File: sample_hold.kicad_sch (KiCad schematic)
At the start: 46 parts, among them K21 G6K-2FY, 5V, Q21 AO3400A, Q22 AO3401A, Q23 AO3400A, Q24 AO3400A, Q25 AO3400A, Q26 AO3400A, Q27 AO3400A, Q28 BSS139, Q29 BSS139, U21 OPA828DGN, U22 OPA2197D, U23 TLV9352D

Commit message: More component metadata.
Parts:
- C202, C211: LCSC (none) -> C14858; Stock (none) -> JLC
- C203, C204, C205, C206, C207, C208, C209, C210, C212, D21, D22, D23, L21, Q21, Q22, Q23, Q24, Q25, Q26, Q27, R201, R203, R204, R205, R206, R208, R209, R210, R211, R215, R216, U21: Stock (none) -> JLC
- JP1: Stock (none) -> Board
- K21: Stock (none) -> LCSC?
- Q28, Q29: Stock (none) -> ?; now left out of the parts list
- R202, R266: footprint Resistor_SMD:R_0402_1005Metric -> Resistor_SMD:R_0603_1608Metric; LCSC (none) -> C25811; Stock (none) -> JLC
- R212: LCSC (none) -> C4190; Stock (none) -> JLC
- R213: LCSC (none) -> C25819; Stock (none) -> JLC
- R214: LCSC (none) -> C4211; Stock (none) -> JLC
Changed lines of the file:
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@@
 			)
 		)
-		(property "Stock" ""
+		(property "Stock" "JLC"
 			(at 177.8 36.83 0)
 			(effects
@@
 			)
 		)
-		(property "Stock" ""
+		(property "Stock" "JLC"
 			(at 106.68 39.37 0)
 			(effects
@@
 			)
 		)
-		(property "Stock" ""
+		(property "Stock" "JLC"
 			(at 161.29 83.82 0)
 			(effects
@@
 			)
 		)
-		(property "Stock" ""
+		(property "Stock" "JLC"
 			(at 85.09 77.47 90)
 			(effects
@@
 			)
 		)
-		(property "Stock" ""
+		(property "Stock" "JLC"
 			(at 78.74 31.75 0)
 			(effects
@@
 			)
 		)
-		(property "Footprint" "Resistor_SMD:R_0402_1005Metric"
+		(property "Footprint" "Resistor_SMD:R_0603_1608Metric"
 			(at 113.03 75.692 90)
 			(effects
@@
 			)
 		)
-		(property "LCSC" ""
+		(property "LCSC" "C25811"
 			(at 113.03 77.47 90)
 			(effects
@@
 			)
 		)
-		(property "Stock" ""
+		(property "Stock" "JLC"
 			(at 113.03 77.47 90)
 			(effects
@@
 			)
 		)
-		(property "Stock" ""
+		(property "Stock" "JLC"
 			(at 78.74 39.37 0)
 			(effects
@@
 			)
 		)
-		(property "Stock" ""
+		(property "Stock" "JLC"
 			(at 156.21 31.75 0)
 			(effects
@@
 		(unit 1)
 		(exclude_from_sim no)
-		(in_bom yes)
+		(in_bom no)
 		(on_board yes)
 		(dnp no)
@@
 			)
 		)
+		(property "Stock" "?"
+			(at 173.99 68.58 90)
+			(effects
+				(font
+					(size 1.27 1.27)
+				)
+				(hide yes)
+			)
+		)
 		(pin "2"
 		)
@@
 			)
 		)
-		(property "LCSC" ""
+		(property "LCSC" "C4211"
 			(at 127 90.17 90)
 			(effects
@@
 			)
 		)
-		(property "Stock" ""
+		(property "Stock" "JLC"
 			(at 127 90.17 90)
 			(effects
@@
 			)
 		)
-		(property "Stock" ""
+		(property "Stock" "JLC"
 			(at 74.93 105.41 0)
 			(effects
@@
 			)
 		)
-		(property "Stock" ""
+		(property "Stock" "JLC"
 			(at 96.52 97.79 90)
 			(effects
@@
 			)
 		)
-		(property "Stock" ""
+		(property "Stock" "JLC"
 			(at 170.18 41.91 0)
 			(effects
@@
 			)
 		)
-		(property "Stock" ""
+		(property "Stock" "Board"
 			(at 92.71 92.71 0)
 			(effects
@@
 			)
 		)
-		(property "Stock" ""
+		(property "Stock" "JLC"
 			(at 138.43 63.5 90)
 			(effects
@@
 			)
 		)
-		(property "Footprint" "Resistor_SMD:R_0402_1005Metric"
+		(property "Footprint" "Resistor_SMD:R_0603_1608Metric"
 			(at 113.03 54.102 90)
 			(effects
@@
 			)
 		)
-		(property "LCSC" ""
+		(property "LCSC" "C25811"
 			(at 113.03 55.88 90)
 			(effects
@@
 			)
 		)
-		(property "Stock" ""
+		(property "Stock" "JLC"
 			(at 113.03 55.88 90)
 			(effects
@@
 			)
 		)
-		(property "LCSC" ""
+		(property "LCSC" "C14858"
 			(at 105.41 73.66 0)
 			(effects
@@
 			)
 		)
-		(property "Stock" ""
+		(property "Stock" "JLC"
 			(at 105.41 73.66 0)
 			(effects
@@
 			)
 		)
-		(property "Stock" ""
+		(property "Stock" "LCSC?"
 			(at 151.13 74.93 90)
 			(effects
@@
 			)
 		)
-		(property "Stock" ""
+		(property "Stock" "JLC"
 			(at 215.9 78.74 90)
 			(effects
@@
 			)
 		)
-		(property "Stock" ""
+		(property "Stock" "JLC"
 			(at 181.61 66.04 90)
 			(effects
@@
 			)
 		)
-		(property "Stock" ""
+		(property "Stock" "LCSC?"
 			(at 156.21 63.5 90)
 			(effects
@@
 			)
 		)
-		(property "Stock" ""
+		(property "Stock" "JLC"
 			(at 184.15 41.91 0)
 			(effects
@@
 			)
 		)
-		(property "Stock" ""
+		(property "Stock" "JLC"
 			(at 100.33 31.75 0)
 			(effects
@@
 			)
 		)
-		(property "Stock" ""
+		(property "Stock" "JLC"
 			(at 138.43 69.85 90)
 			(effects
@@
 			)
 		)
-		(property "Stock" ""
+		(property "Stock" "JLC"
 			(at 181.61 31.75 90)
 			(effects
@@
 			)
 		)
-		(property "LCSC" ""
+		(property "LCSC" "C25819"
 			(at 114.3 97.79 90)
 			(effects
@@
 			)
 		)
-		(property "Stock" ""
+		(property "Stock" "JLC"
 			(at 114.3 97.79 90)
 			(effects
@@
 			)
 		)
-		(property "Stock" ""
+		(property "Stock" "JLC"
 			(at 106.68 31.75 0)
 			(effects
@@
 			)
 		)
-		(property "Stock" ""
+		(property "Stock" "JLC"
 			(at 161.29 91.44 0)
 			(effects
@@
 			)
 		)
-		(property "Stock" ""
+		(property "Stock" "JLC"
 			(at 171.45 83.82 0)
 			(effects
@@
 			)
 		)
-		(property "Stock" ""
+		(property "Stock" "LCSC?"
 			(at 156.21 41.91 90)
 			(effects
@@
 			)
 		)
-		(property "Stock" ""
+		(property "Stock" "JLC"
 			(at 215.9 68.58 90)
 			(effects
@@
 			)
 		)
-		(property "Stock" ""
+		(property "Stock" "JLC"
 			(at 189.23 31.75 0)
 			(effects
@@
 			)
 		)
-		(property "LCSC" ""
+		(property "LCSC" "C4190"
 			(at 101.6 92.71 90)
 			(effects
@@
 			)
 		)
-		(property "Stock" ""
+		(property "Stock" "JLC"
 			(at 101.6 92.71 90)
 			(effects
@@
 			)
 		)
-		(property "Stock" ""
+		(property "Stock" "JLC"
 			(at 170.18 27.94 90)
 			(effects
@@
 			)
 		)
-		(property "Stock" ""
+		(property "Stock" "JLC"
 			(at 142.24 41.91 0)
 			(effects
@@
 			)
 		)
-		(property "Stock" ""
+		(property "Stock" "JLC"
 			(at 100.33 39.37 0)
 			(effects
@@
 			)
 		)
-		(property "Stock" ""
+		(property "Stock" "JLC"
 			(at 187.96 45.72 90)
 			(effects
@@
 			)
 		)
-		(property "Stock" ""
+		(property "Stock" "JLC"
 			(at 203.2 68.58 0)
 			(effects
@@
 			)
 		)
-		(property "Stock" ""
+		(property "Stock" "JLC"
 			(at 138.43 58.42 90)
 			(effects
@@
 			)
 		)
-		(property "Stock" ""
+		(property "Stock" "JLC"
 			(at 171.45 91.44 0)
 			(effects
@@
 			)
 		)
-		(property "Stock" ""
+		(property "Stock" "JLC"
 			(at 74.93 97.79 0)
 			(effects
@@
 			)
 		)
-		(property "LCSC" ""
+		(property "LCSC" "C14858"
 			(at 210.82 73.66 0)
 			(effects
@@
 			)
 		)
-		(property "Stock" ""
+		(property "Stock" "JLC"
 			(at 210.82 73.66 0)
 			(effects
@@
 			)
 		)
-		(property "Stock" ""
+		(property "Stock" "JLC"
 			(at 138.43 74.93 90)
 			(effects
@@
 			)
 		)
-		(property "Stock" ""
+		(property "Stock" "JLC"
 			(at 134.62 45.72 0)
 			(effects
@@
 		(unit 1)
 		(exclude_from_sim no)
-		(in_bom yes)
+		(in_bom no)
 		(on_board yes)
 		(dnp no)
@@
 			(effects
 				(font
+					(size 1.27 1.27)
+				)
+				(hide yes)
+			)
+		)
+		(property "Stock" "?"
+			(at 189.23 63.5 90)
+			(effects
+				(font

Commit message: Front panel
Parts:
- C211: value 0n1 -> 10n; LCSC C14858 -> C307500
- R201: value 16k -> 15k; footprint Resistor_SMD:R_0603_1608Metric -> Resistor_SMD:R_0402_1005Metric; LCSC C22818 -> C25756
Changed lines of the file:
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@@
 			)
 		)
-		(property "Value" "16k"
+		(property "Value" "15k"
 			(at 85.09 77.47 90)
 			(effects
@@
 			)
 		)
-		(property "Footprint" "Resistor_SMD:R_0603_1608Metric"
+		(property "Footprint" "Resistor_SMD:R_0402_1005Metric"
 			(at 85.09 75.692 90)
 			(effects
@@
 			)
 		)
-		(property "LCSC" "C22818"
+		(property "LCSC" "C25756"
 			(at 85.09 77.47 90)
 			(effects
@@
 			)
 		)
-		(property "Value" "0n1"
+		(property "Value" "10n"
 			(at 210.82 75.692 0)
 			(effects
@@
 			)
 		)
-		(property "LCSC" "C14858"
+		(property "LCSC" "C307500"
 			(at 210.82 73.66 0)
 			(effects

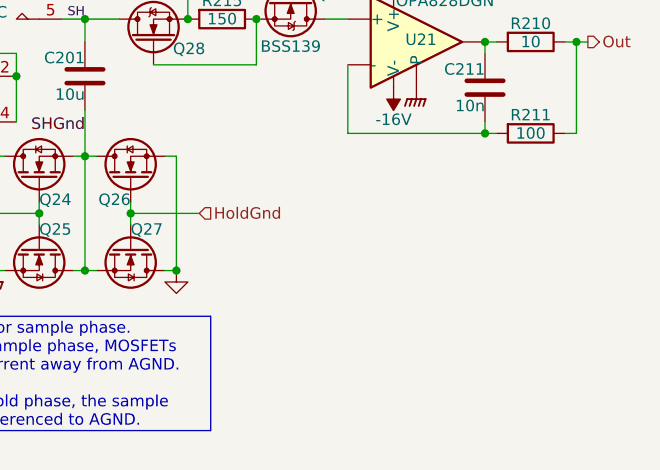
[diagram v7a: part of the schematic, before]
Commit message: Change some footprints.
Mounting holes for covers.
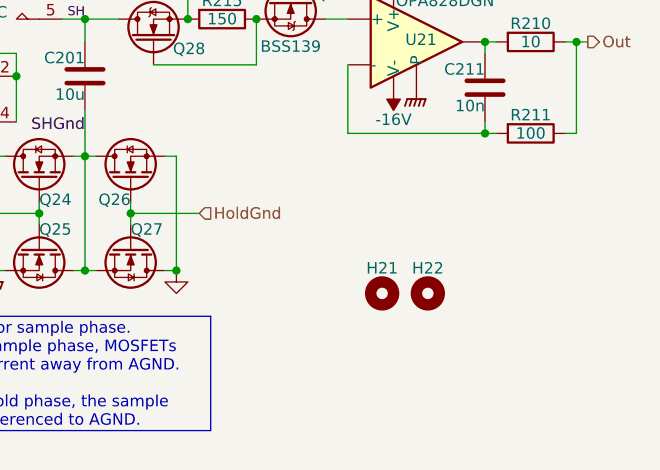
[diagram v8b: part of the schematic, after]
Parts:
- added H21, H22: MountingHole, Parts:Hole_1.5mm_Unplated, symbol Mechanical:MountingHole
- U21: footprint Parts:OPA828DGN -> Parts:SOIC-8_3.9x4.9mm_EP; Stock JLC -> (none); now left out of the parts list
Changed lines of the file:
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@@
+	)
+	(symbol
+		(lib_id "Mechanical:MountingHole")
+		(at 204.47 96.52 0)
+		(unit 1)
+		(exclude_from_sim no)
+		(in_bom no)
+		(on_board yes)
+		(dnp no)
+		(property "Reference" "H22"
+			(at 204.47 93.726 0)
+			(effects
+				(font
+					(size 1.27 1.27)
+				)
+			)
+		)
+		(property "Value" "MountingHole"
+			(at 204.47 93.345 0)
+			(effects
+				(font
+					(size 1.27 1.27)
+				)
+				(hide yes)
+			)
+		)
+		(property "Footprint" "Parts:Hole_1.5mm_Unplated"
+			(at 204.47 96.52 0)
+			(effects
+				(font
+					(size 1.27 1.27)
+				)
+				(hide yes)
+			)
+		)
+		(property "Datasheet" "~"
+			(at 204.47 96.52 0)
+			(effects
+				(font
+					(size 1.27 1.27)
+				)
+				(hide yes)
+			)
+		)
+		(property "Description" "Mounting Hole without connection"
+			(at 204.47 96.52 0)
+			(effects
+				(font
+					(size 1.27 1.27)
+				)
+				(hide yes)
+			)
+		)
+		(instances
+			(project "lincal"
+				(path "/b054cef4-39e3-49d8-aff0-7ba5a206c187/6f91b1d1-06a0-428d-b546-bc9bd4fa19a0"
+					(reference "H26")
+					(unit 1)
+				)
+				(path "/b054cef4-39e3-49d8-aff0-7ba5a206c187/8eaf15be-2df7-401b-a518-33a048754894"
+					(reference "H22")
+					(unit 1)
+				)
+			)
+		)
 	)
 	(symbol
@@
 		(unit 1)
 		(exclude_from_sim no)
-		(in_bom yes)
+		(in_bom no)
 		(on_board yes)
 		(dnp no)
@@
 			)
 		)
-		(property "Footprint" "Parts:OPA828DGN"
+		(property "Footprint" "Parts:SOIC-8_3.9x4.9mm_EP"
 			(at 200.66 73.66 0)
 			(effects
@@
 			)
 		)
-		(property "Stock" "JLC"
+		(property "Stock" ""
 			(at 203.2 68.58 0)
 			(effects
@@
 					(unit 1)
 				)
+			)
+		)
+	)
+	(symbol
+		(lib_id "Mechanical:MountingHole")
+		(at 199.39 96.52 0)
+		(unit 1)
+		(exclude_from_sim no)
+		(in_bom no)
+		(on_board yes)
+		(dnp no)
+		(property "Reference" "H21"
+			(at 199.39 93.726 0)
+			(effects
+				(font
+					(size 1.27 1.27)
+				)
+			)
+		)
+		(property "Value" "MountingHole"
+			(at 199.39 93.345 0)
+			(effects
+				(font
+					(size 1.27 1.27)
+				)
+				(hide yes)
+			)
+		)
+		(property "Footprint" "Parts:Hole_1.5mm_Unplated"
+			(at 199.39 96.52 0)
+			(effects
+				(font
+					(size 1.27 1.27)
+				)
+				(hide yes)
+			)
+		)
+		(property "Datasheet" "~"
+			(at 199.39 96.52 0)
+			(effects
+				(font
+					(size 1.27 1.27)
+				)
+				(hide yes)
+			)
+		)
+		(property "Description" "Mounting Hole without connection"
+			(at 199.39 96.52 0)
+			(effects
+				(font
+					(size 1.27 1.27)
+				)
+				(hide yes)
+			)
+		)
+		(instances
+			(project ""
+				(path "/b054cef4-39e3-49d8-aff0-7ba5a206c187/6f91b1d1-06a0-428d-b546-bc9bd4fa19a0"
+					(reference "H25")
+					(unit 1)
+				)
+				(path "/b054cef4-39e3-49d8-aff0-7ba5a206c187/8eaf15be-2df7-401b-a518-33a048754894"
+					(reference "H21")
+					(unit 1)
+				)
